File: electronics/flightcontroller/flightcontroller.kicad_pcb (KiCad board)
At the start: 2 copper layers, 30 x 50 mm, 67 parts, among them J1 BATT, J10 USB, J2 ESC+, J3 ESC, J4 Servo3, J5 Servo2, J6 Servo1, J7 ESC-, J8 Micro_SD_Card_Det_HYC80-TF08-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, J9 SWD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

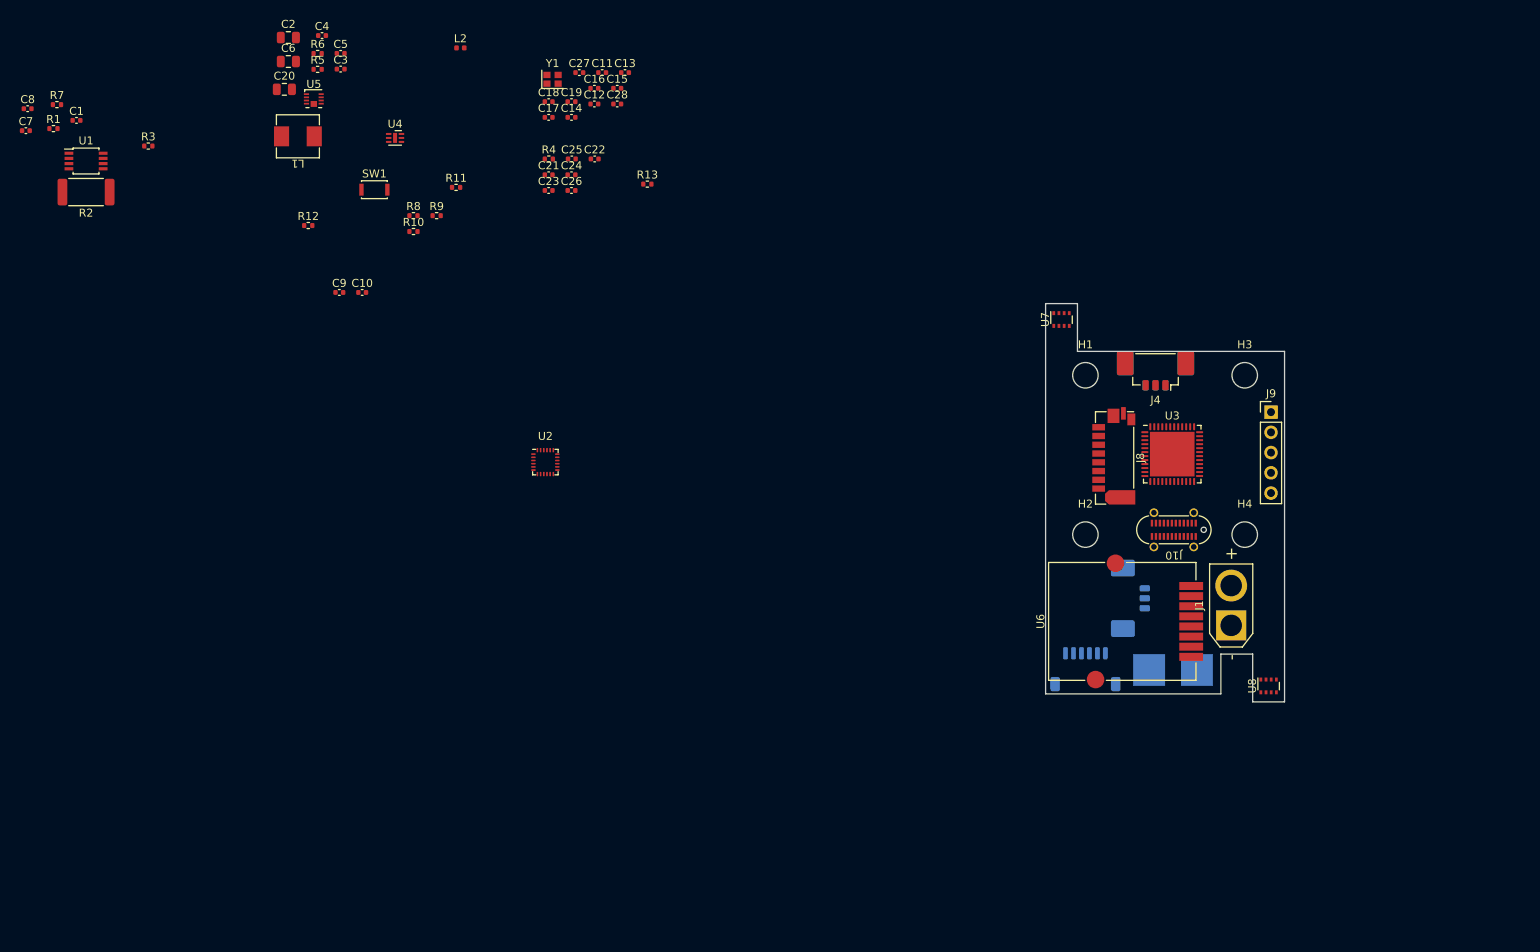
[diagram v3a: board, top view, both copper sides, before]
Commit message: electronics: Microcontroller connections, general component placement.
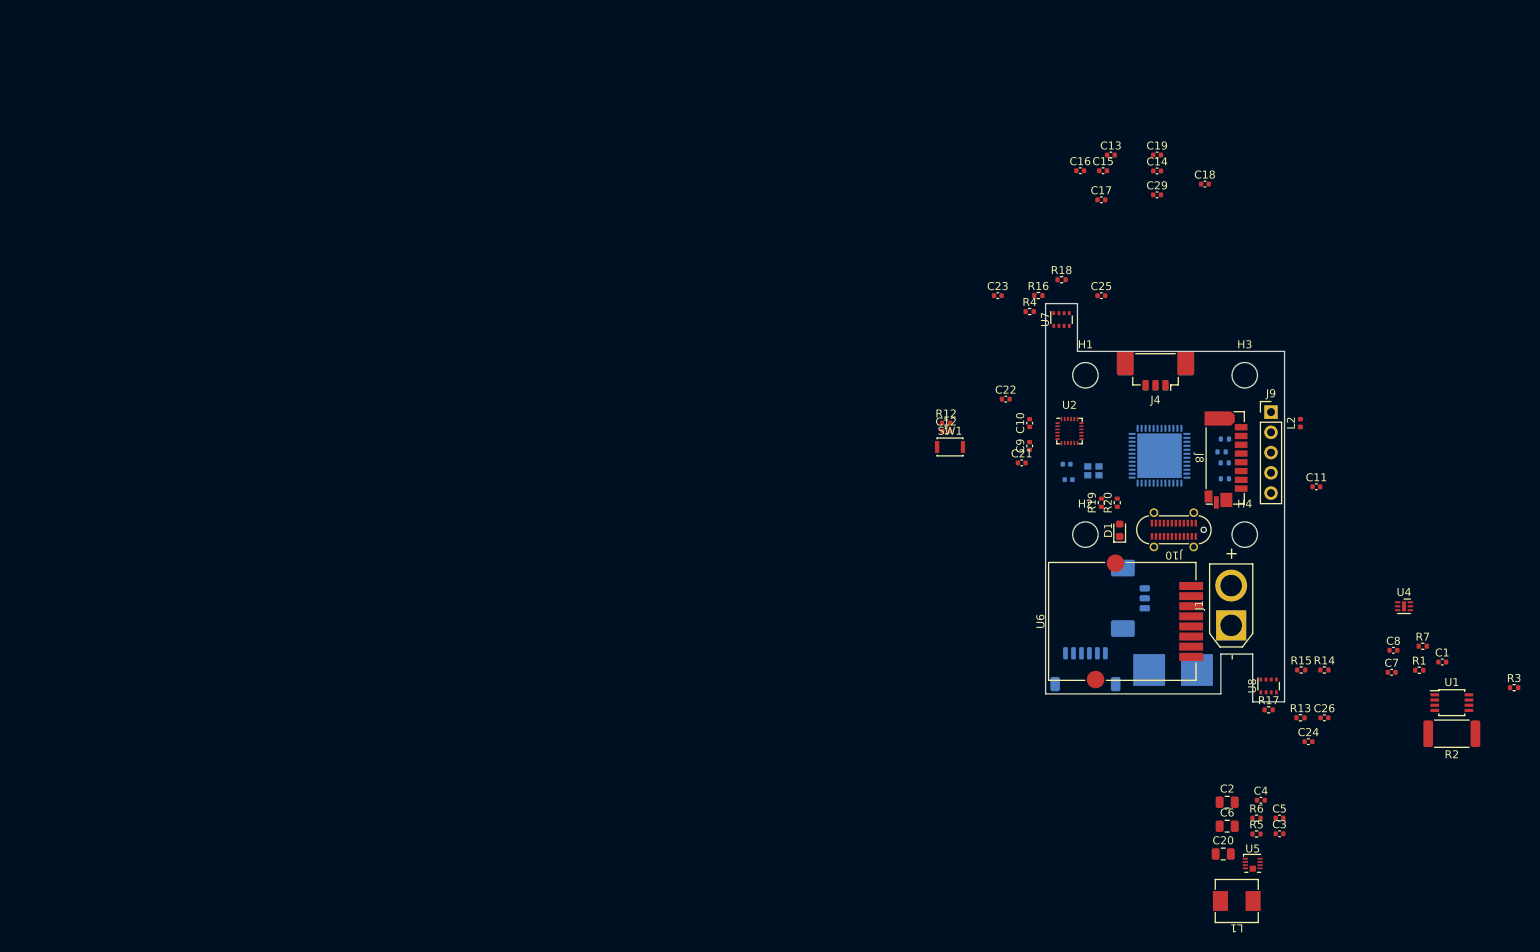
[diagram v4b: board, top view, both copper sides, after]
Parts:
- added C29: 0.1uF, Capacitor_SMD:C_0402_1005Metric, F.Cu at (199.0, 47.4)
- added D1: LED, LED_SMD:LED_0603_1608Metric, F.Cu at (194.3, 89.5)
- added R14: 4.7k, Resistor_SMD:R_0402_1005Metric, F.Cu at (220.0, 107.0)
- added R15: 4.7k, Resistor_SMD:R_0402_1005Metric, F.Cu at (217.1, 107.0)
- added R16: 4.7k, Resistor_SMD:R_0402_1005Metric, F.Cu at (184.1, 60.0)
- added R17: 10k, Resistor_SMD:R_0402_1005Metric, F.Cu at (213.0, 112.0)
- added R18: 4.7k, Resistor_SMD:R_0402_1005Metric, F.Cu at (187.0, 58.0)
- added R19: 47k, Resistor_SMD:R_0402_1005Metric, F.Cu at (192.0, 86.0)
- added R20: 1k, Resistor_SMD:R_0402_1005Metric, F.Cu at (194.0, 86.0)
- C27, C28, R10, R11, R8, R9, Y1: moved to B.Cu
- U3: value STM32L462CEUx -> STM32G491CCUx; moved to B.Cu
- moved C1 184.5 mm to (234.8, 106.0)
- moved C7 184.5 mm to (228.4, 107.3)
- moved R1 184.5 mm to (231.9, 107.0)
- moved R2 184.5 mm to (236.0, 115.0)
- moved R3 184.5 mm to (243.8, 109.2)
- moved R7 184.5 mm to (232.3, 104.0)
- moved U1 184.5 mm to (236.0, 111.1)
- moved C8 184.5 mm to (228.7, 104.5)
- moved C2 152.0 mm to (207.8, 123.6)
- moved C20 152.0 mm to (207.3, 130.1)
- moved C3 152.0 mm to (214.4, 127.6)
- moved C4 152.0 mm to (212.0, 123.3)
- moved C5 152.0 mm to (214.4, 125.6)
- moved C6 152.0 mm to (207.8, 126.6)
- moved L1 152.0 mm to (209.0, 136.0)
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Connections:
- J3 pad 1: unconnected-(J3-Pad1) -> /MCU/PWM_M4
- J3 pad 2: unconnected-(J3-Pad2) -> /MCU/PWM_M3
- J3 pad 3: unconnected-(J3-Pad3) -> /MCU/PWM_M2
- J3 pad 4: unconnected-(J3-Pad4) -> /MCU/PWM_M1
- J3 pad 5: unconnected-(J3-Pad5) -> +3V3
- J3 pad 6: unconnected-(J3-Pad6) -> GND
- J4 pad 1: unconnected-(J4-Pad1) -> /MCU/SERVO_ELEV
- J4 pad 2: unconnected-(J4-Pad2) -> +4V
- J4 pad 3: unconnected-(J4-Pad3) -> GND
- J5 pad 1: unconnected-(J5-Pad1) -> /MCU/SERVO_ENG
- J5 pad 2: unconnected-(J5-Pad2) -> +4V
- J5 pad 3: unconnected-(J5-Pad3) -> GND
- J6 pad 1: unconnected-(J6-Pad1) -> /MCU/SERVO_RUD
- J6 pad 2: unconnected-(J6-Pad2) -> +4V
- J6 pad 3: unconnected-(J6-Pad3) -> GND
- U1 pad 1: /Power Management/SCL -> /MCU/PWR_SCL
- U1 pad 2: /Power Management/SDA -> /MCU/PWR_SDA
- U2 pad 11: /Sensors/IMU_FSYNC -> /MCU/IMU_FSYNC
- U2 pad 12: /Sensors/IMU_INT -> /MCU/IMU_INT
- U2 pad 22: /Sensors/IMU_~{CS} -> /MCU/IMU_~{CS}
- U2 pad 23: /Sensors/IMU_SCLK -> /MCU/IMU_SCLK
- U2 pad 24: /Sensors/IMU_MOSI -> /MCU/IMU_MOSI
- U2 pad 9: /Sensors/IMU_MISO -> /MCU/IMU_MISO
- U3 pad 10: unconnected-(U3-Pad10) -> /MCU/PWM_M3
- U3 pad 11: unconnected-(U3-Pad11) -> /MCU/PWM_M4
- U3 pad 12: unconnected-(U3-Pad12) -> /MCU/IMU_INT
- U3 pad 13: unconnected-(U3-Pad13) -> /MCU/IMU_SCLK
- U3 pad 14: unconnected-(U3-Pad14) -> /MCU/IMU_MISO
- U3 pad 15: unconnected-(U3-Pad15) -> /MCU/IMU_MOSI
- U3 pad 16: unconnected-(U3-Pad16) -> /MCU/IMU_~{CS}
- U3 pad 17: unconnected-(U3-Pad17) -> /MCU/SERVO_RUD
- U3 pad 18: unconnected-(U3-Pad18) -> /MCU/SERVO_ELEV
- U3 pad 19: unconnected-(U3-Pad19) -> /MCU/PR_RST
- U3 pad 2: unconnected-(U3-Pad2) -> /MCU/RADIO_CE
- U3 pad 20: unconnected-(U3-Pad20) -> +3V3
- U3 pad 21: unconnected-(U3-Pad21) -> +3V3
- U3 pad 22: unconnected-(U3-Pad22) -> /MCU/GPS_TX
- U3 pad 23: GND -> +3V3
- U3 pad 24: +3V3 -> /MCU/GPS_RX
- U3 pad 25: unconnected-(U3-Pad25) -> /MCU/SD_DET
- U3 pad 26: unconnected-(U3-Pad26) -> /MCU/SD_SCK
- U3 pad 27: unconnected-(U3-Pad27) -> /MCU/SD_MISO
- U3 pad 28: unconnected-(U3-Pad28) -> /MCU/SD_MOSI
- U3 pad 29: unconnected-(U3-Pad29) -> /MCU/RADIO_~{CS}
- U3 pad 3: unconnected-(U3-Pad3) -> /MCU/RADIO_~{IRQ}
- U3 pad 30: unconnected-(U3-Pad30) -> /MCU/PWR_SDA
- U3 pad 31: unconnected-(U3-Pad31) -> /MCU/PWR_SCL
- U3 pad 32: unconnected-(U3-Pad32) -> /MCU/SD_CS
- U3 pad 33: unconnected-(U3-Pad33) -> /MCU/USBN
- U3 pad 34: unconnected-(U3-Pad34) -> /MCU/USBP
- U3 pad 35: GND -> +3V3
- U3 pad 36: +3V3 -> /MCU/SWDIO
- U3 pad 37: unconnected-(U3-Pad37) -> /MCU/SWCLK
- U3 pad 38: unconnected-(U3-Pad38) -> /MCU/PR_SCL
- U3 pad 39: unconnected-(U3-Pad39) -> /MCU/RADIO_SCK
- U3 pad 4: unconnected-(U3-Pad4) -> /MCU/IMU_FSYNC
- U3 pad 40: unconnected-(U3-Pad40) -> /MCU/RADIO_MISO
- U3 pad 41: unconnected-(U3-Pad41) -> /MCU/SWO
- U3 pad 42: unconnected-(U3-Pad42) -> /MCU/SERVO_ENG
- U3 pad 43: unconnected-(U3-Pad43) -> /MCU/RADIO_MOSI
- U3 pad 44: unconnected-(U3-Pad44) -> /MCU/PAYLOAD_TX
- U3 pad 45: unconnected-(U3-Pad45) -> /MCU/PAYLOAD_RX
- U3 pad 46: unconnected-(U3-Pad46) -> Net-(R19-Pad1)
- U3 pad 47: GND -> /MCU/PR_SDA
- U3 pad 5: unconnected-(U3-Pad5) -> /MCU/OSCB
- U3 pad 6: unconnected-(U3-Pad6) -> /MCU/OSCA
- U3 pad 8: GND -> /MCU/PWM_M1
- U3 pad 9: +3V3 -> /MCU/PWM_M2
- U7 pad 1: /Sensors/PR_RST -> /MCU/PR_RST
- U7 pad 3: /Sensors/PR_SDA -> /MCU/PR_SDA
- U7 pad 4: /Sensors/PR_SCL -> /MCU/PR_SCL
- U8 pad 1: /Sensors/PR_RST -> /MCU/PR_RST
- U8 pad 3: /Sensors/PR_SDA -> /MCU/PR_SDA
- U8 pad 4: /Sensors/PR_SCL -> /MCU/PR_SCL

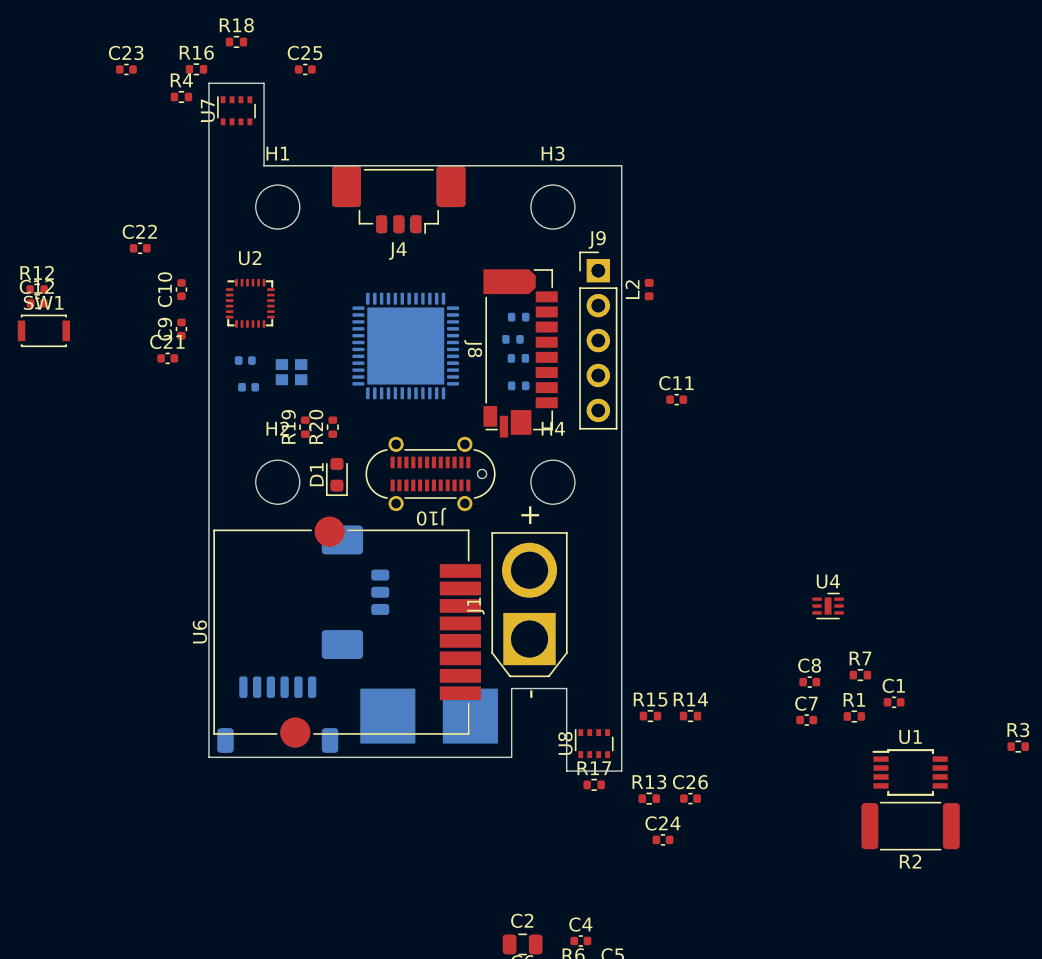
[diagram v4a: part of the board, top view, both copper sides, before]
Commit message: electronics: Fix remaining schematics ERC errors.
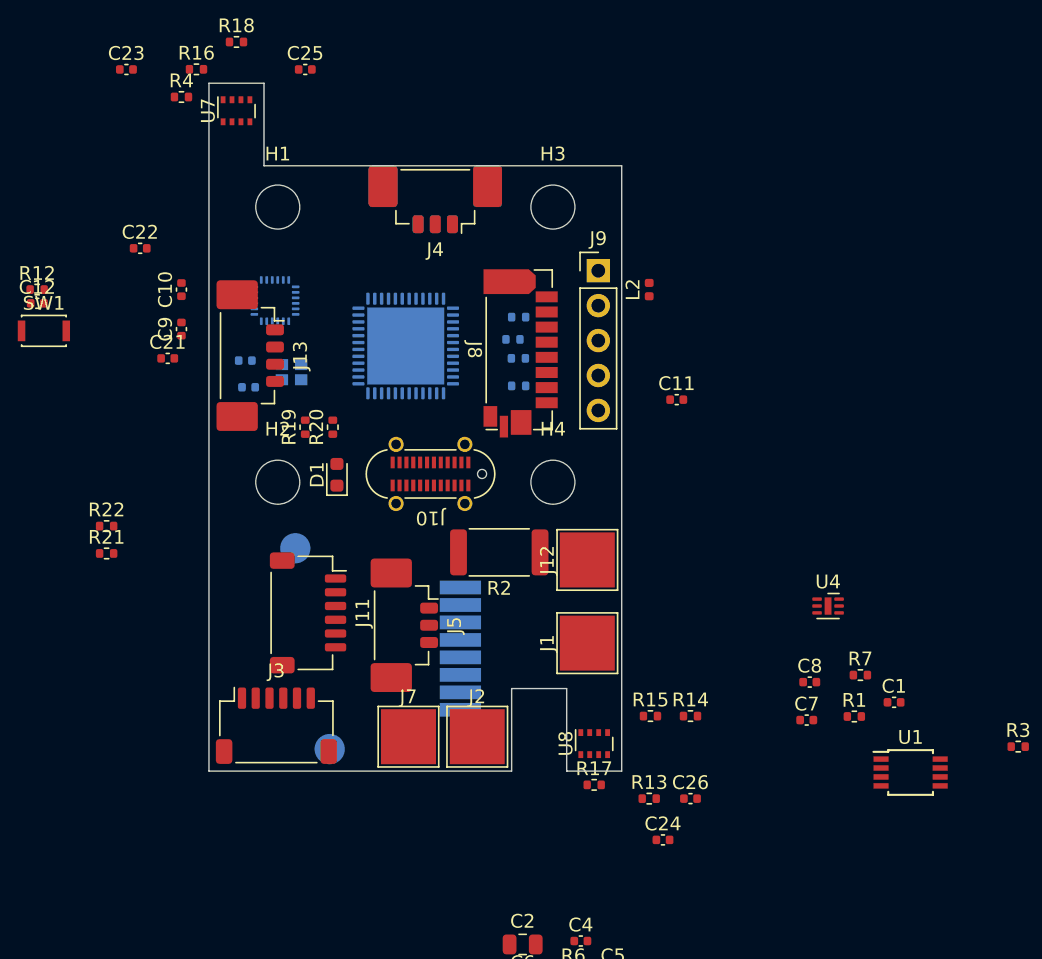
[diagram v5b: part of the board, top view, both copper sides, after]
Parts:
- added J11: Payload, Connector_JST:JST_SH_SM06B-SRSS-TB_1x06-1MP_P1.00mm_Horizontal, F.Cu at (192.2, 99.5)
- added J12: BAT-, TestPoint:TestPoint_Pad_4.0x4.0mm, F.Cu at (212.5, 95.7)
- added J13: Conn_01x04, Connector_Molex:Molex_PicoBlade_53398-0471_1x04-1MP_P1.25mm_Vertical, F.Cu at (188.6, 80.8)
- added R21: 5.1k, Resistor_SMD:R_0402_1005Metric, F.Cu at (177.6, 95.2)
- added R22: 5.1k, Resistor_SMD:R_0402_1005Metric, F.Cu at (177.6, 93.2)
- J1: value BATT -> BAT+; footprint Connector_AMASS:AMASS_XT30U-F_1x02_P5.0mm_Vertical -> TestPoint:TestPoint_Pad_4.0x4.0mm
- J2, J3, J5, J7: moved to F.Cu
- U2, U6: moved to B.Cu
- moved R2 35.9 mm to (206.1, 95.1)
- moved J5 4.29 mm to (199.8, 100.4), turned to -90 degrees
- moved J1 4.21 mm to (212.5, 101.7)
- moved J4 2.65 mm to (201.4, 70.0)
- moved J6 2.65 mm to (201.4, 70.0)
- moved J7 2.12 mm to (199.5, 108.5), turned to 0 degrees
- moved U2 1.81 mm to (189.8, 76.8), turned to 180 degrees
- moved J2 1.58 mm to (204.5, 108.5), turned to 0 degrees
- moved U6 1.20 mm to (194.6, 102.1), turned to -90 degrees
- moved J3 0.81 mm to (189.9, 107.7), turned to 0 degrees
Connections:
- C10 pad 2: unconnected-(C10-Pad2) -> GND
- J1 pad 1: Net-(C1-Pad2) -> +BATT
- J10 pad A1: Net-(J10-PadA1) -> GND
- J10 pad A12: Net-(J10-PadA1) -> GND
- J10 pad A5: unconnected-(J10-PadA5) -> Net-(J10-PadA5)
- J10 pad A6: unconnected-(J10-PadA6) -> /MCU/USBP
- J10 pad A7: unconnected-(J10-PadA7) -> /MCU/USBN
- J10 pad B1: Net-(J10-PadA1) -> GND
- J10 pad B12: Net-(J10-PadA1) -> GND
- J10 pad B5: unconnected-(J10-PadB5) -> Net-(J10-PadB5)
- J10 pad B6: unconnected-(J10-PadB6) -> /MCU/USBP
- J10 pad B7: unconnected-(J10-PadB7) -> /MCU/USBN
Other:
- outline, holes or cut-outs redrawn
- board text added: "TODO: - Reset switch footprint"

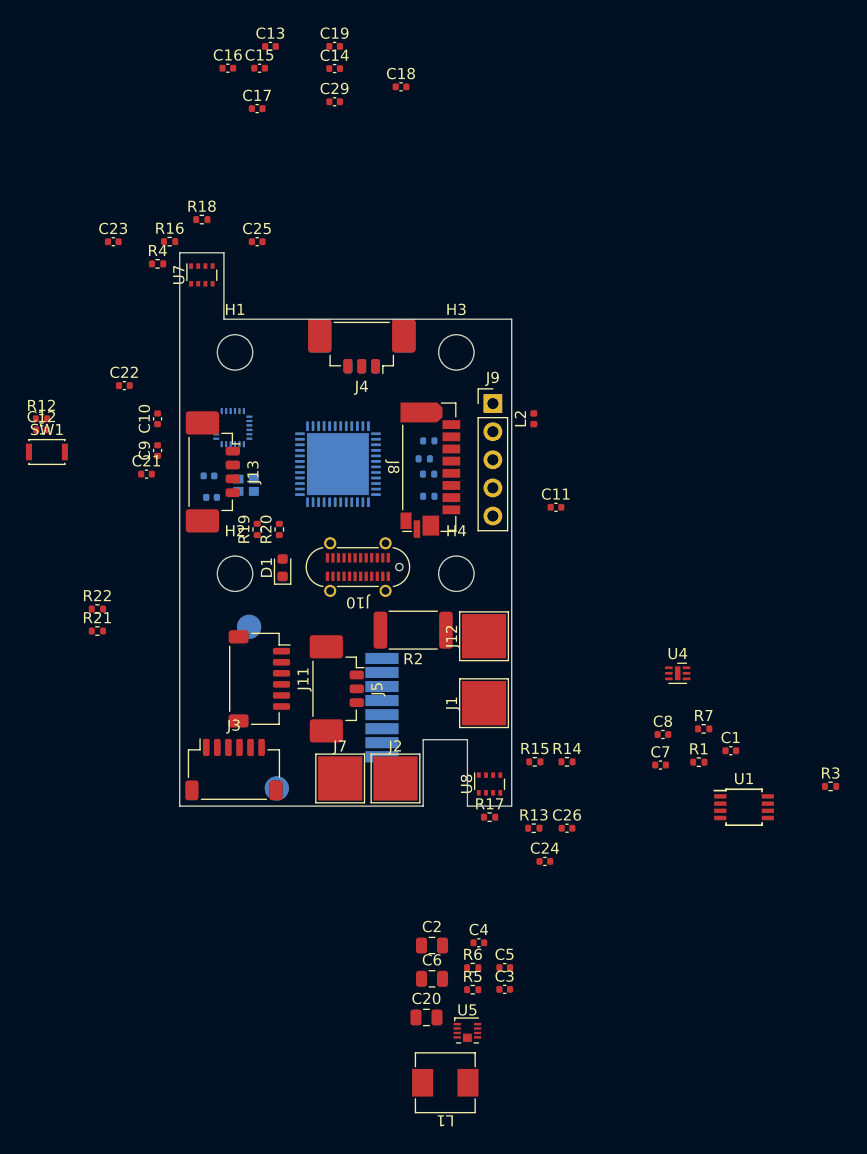
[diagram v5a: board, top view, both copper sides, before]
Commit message: electronics: Preliminary component placement.
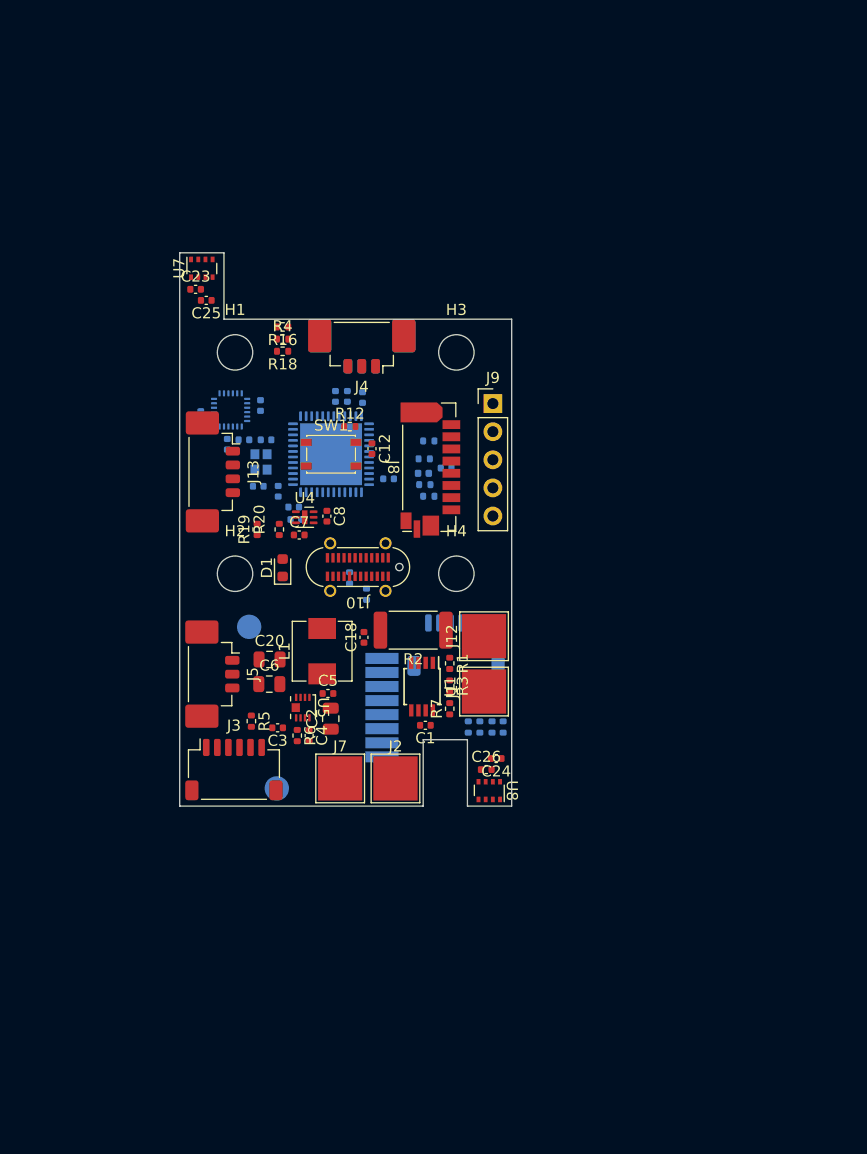
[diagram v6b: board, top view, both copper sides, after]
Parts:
- C10, C11, C13, C14, C15, C16, C17, C19, C21, C22, C29, C9, J11, L2, R13, R14, R15, R17, R21, R22: moved to B.Cu
- SW1: footprint Button_Switch_SMD:SW_SPST_CK_KXT3 -> flightcontroller-footprints:SW_SPST_PTS815
- moved C18 49.9 mm to (201.7, 95.8), turned to 90 degrees
- moved C19 42.9 mm to (195.5, 85.1), turned to 180 degrees
- moved L1 40.6 mm to (197.9, 97.0), turned to 90 degrees
- moved C15 39.8 mm to (195.3, 84.0), turned to 180 degrees
- moved C7 38.7 mm to (195.8, 86.5)
- moved C16 38.5 mm to (193.9, 82.5), turned to -90 degrees
- moved C14 37.4 mm to (203.9, 81.4)
- moved U4 36.5 mm to (196.3, 84.9)
- moved C8 36.2 mm to (198.3, 84.8), turned to -90 degrees
- moved R3 35.6 mm to (209.4, 100.2), turned to -90 degrees
- moved C20 35.3 mm to (193.1, 97.8)
- moved U5 32.8 mm to (196.1, 102.1), turned to -90 degrees
- moved C13 32.2 mm to (199.1, 74.0), turned to 90 degrees
- moved R5 31.4 mm to (191.5, 103.3), turned to -90 degrees
- moved C3 31.3 mm to (193.8, 103.9), turned to 180 degrees
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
